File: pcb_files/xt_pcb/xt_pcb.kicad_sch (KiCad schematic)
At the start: 20 parts, among them J1 Conn_01x04_Socket, J2 USB_C_Receptacle_USB2.0_16P, U1 AMS1117-3.3, U2 ATmega32U4-A, U3 USB6B1, Y1 Crystal_GND24_Small

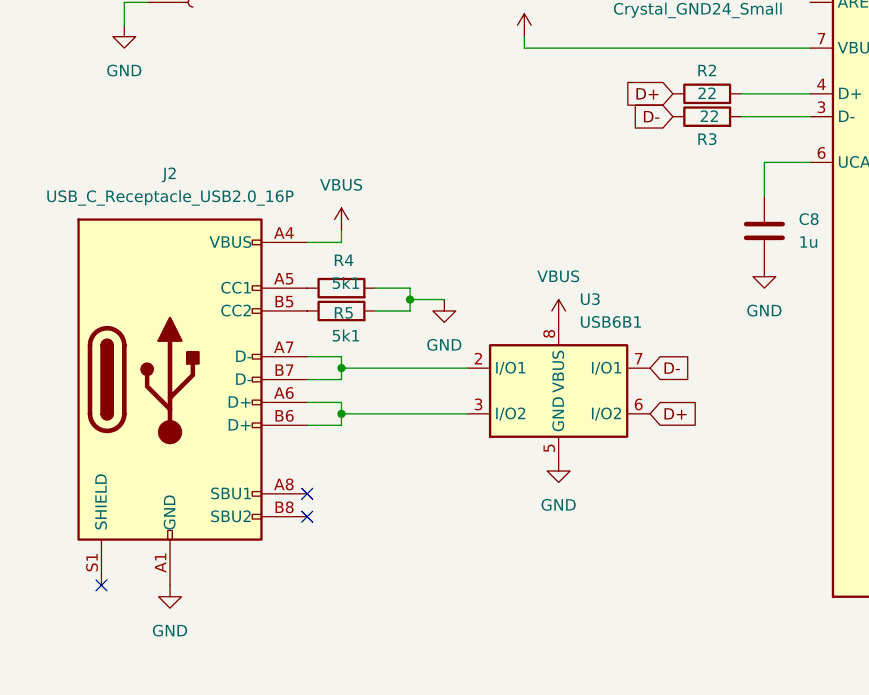
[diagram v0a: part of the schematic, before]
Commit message: finalized files + UDB C4 implementation
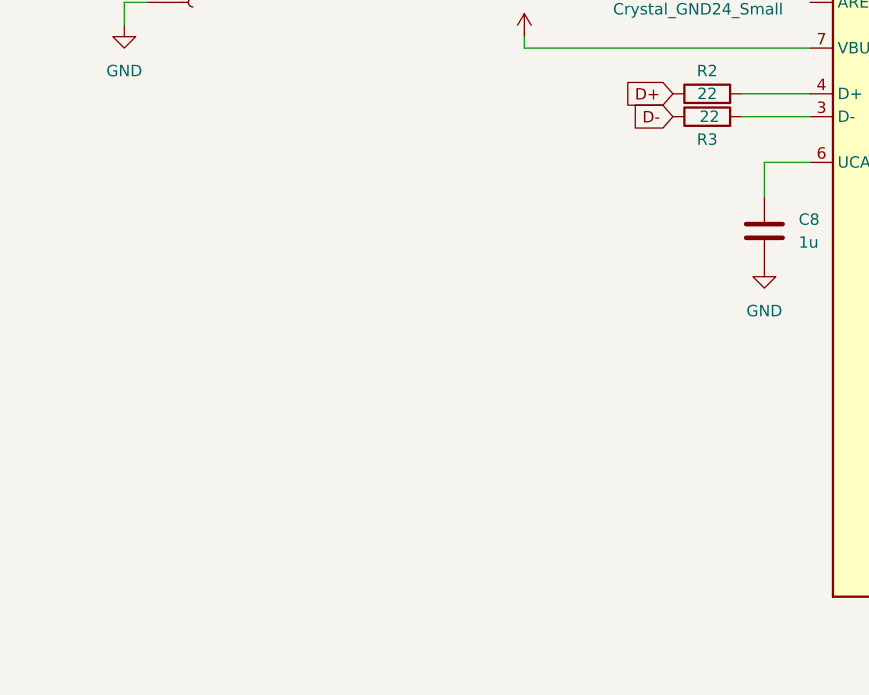
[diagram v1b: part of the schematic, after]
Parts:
- removed J2: USB_C_Receptacle_USB2.0_16P, Connector_USB:USB_C_Receptacle_HRO_TYPE-C-31-M-12, symbol Connector:USB_C_Receptacle_USB2.0_16P
- removed R4, R5: 5k1, Resistor_SMD:R_0402_1005Metric, symbol Device:R
- removed U3: USB6B1, Package_SO:SOIC-8_3.9x4.9mm_P1.27mm, symbol Power_Protection:USB6B1
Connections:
- no-connect marks 3 -> 0

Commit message: basic firmware added
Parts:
- J1: footprint Connector_JST:JST_SH_SM04B-SRSS-TB_1x04-1MP_P1.00mm_Horizontal -> Downloads:MOLEX_781710004
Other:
- moved on the sheet: J1
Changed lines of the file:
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@@
 	(wire
 		(pts
-			(xy 27.94 68.58) (xy 30.48 68.58)
+			(xy 27.94 68.58) (xy 33.02 68.58)
 		)
 		(stroke
@@
 	(wire
 		(pts
-			(xy 30.48 76.2) (xy 27.94 76.2)
+			(xy 33.02 76.2) (xy 27.94 76.2)
+		)
+		(stroke
+			(width 0)
+			(type default)
+		)
+	)
+	(wire
+		(pts
+			(xy 33.02 73.66) (xy 30.48 73.66)
 		)
 		(stroke
@@
 		(pts
 			(xy 29.21 30.48) (xy 29.21 27.94)
+		)
+		(stroke
+			(width 0)
+			(type default)
+		)
+	)
+	(wire
+		(pts
+			(xy 33.02 71.12) (xy 30.48 71.12)
 		)
 		(stroke
@@
 	(symbol
 		(lib_id "Connector:Conn_01x04_Socket")
-		(at 35.56 71.12 0)
+		(at 38.1 71.12 0)
 		(unit 1)
 		(exclude_from_sim no)
@@
 		(dnp no)
 		(property "Reference" "J1"
-			(at 37.592 60.198 0)
+			(at 40.132 60.198 0)
 			(effects
 				(font
@@
 		)
 		(property "Value" "Conn_01x04_Socket"
-			(at 37.592 62.738 0)
-			(effects
-				(font
-					(size 1.27 1.27)
-				)
-				(justify left)
-			)
-		)
-		(property "Footprint" "Connector_JST:JST_SH_SM04B-SRSS-TB_1x04-1MP_P1.00mm_Horizontal"
-			(at 35.56 71.12 0)
-			(effects
-				(font
-					(size 1.27 1.27)
-				)
-				(hide yes)
+			(at 40.132 62.738 0)
+			(effects
+				(font
+					(size 1.27 1.27)
+				)
+				(justify left)
+			)
+		)
+		(property "Footprint" "Downloads:MOLEX_781710004"
+			(at 38.1 71.12 0)
+			(effects
+				(font
+					(size 1.27 1.27)
+				)
 			)
 		)
 		(property "Datasheet" "~"
-			(at 35.56 71.12 0)
+			(at 38.1 71.12 0)
 			(effects
 				(font
@@
 		)
 		(property "Description" "Generic connector, single row, 01x04, script generated"
-			(at 35.56 71.12 0)
-			(effects
-				(font
+			(at 38.1 71.12 0)
+			(effects
+				(font

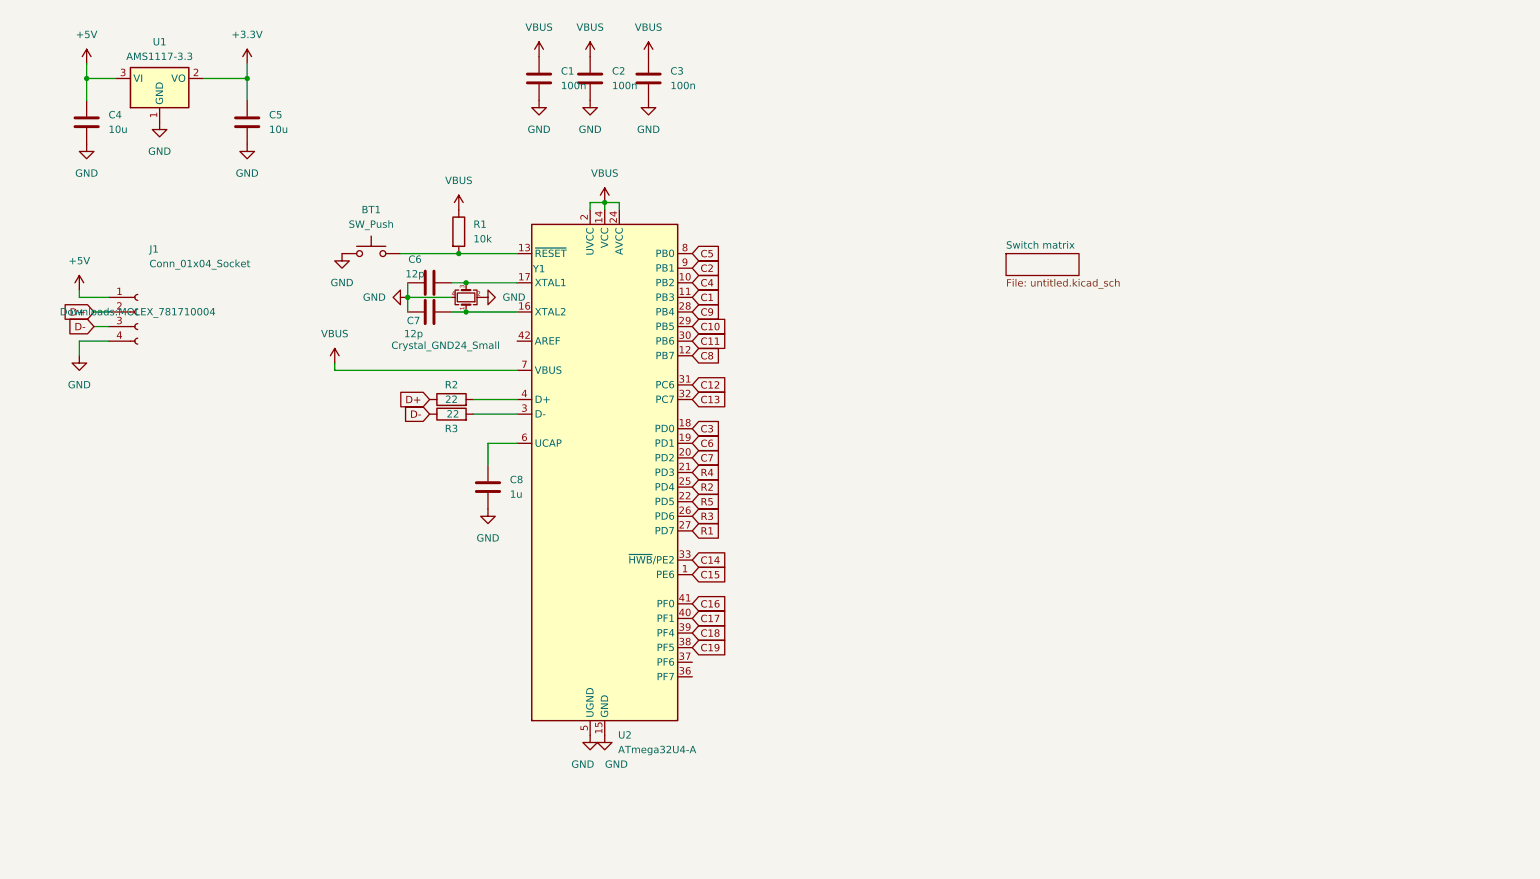
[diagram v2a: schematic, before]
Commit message: new RP2040 pcb
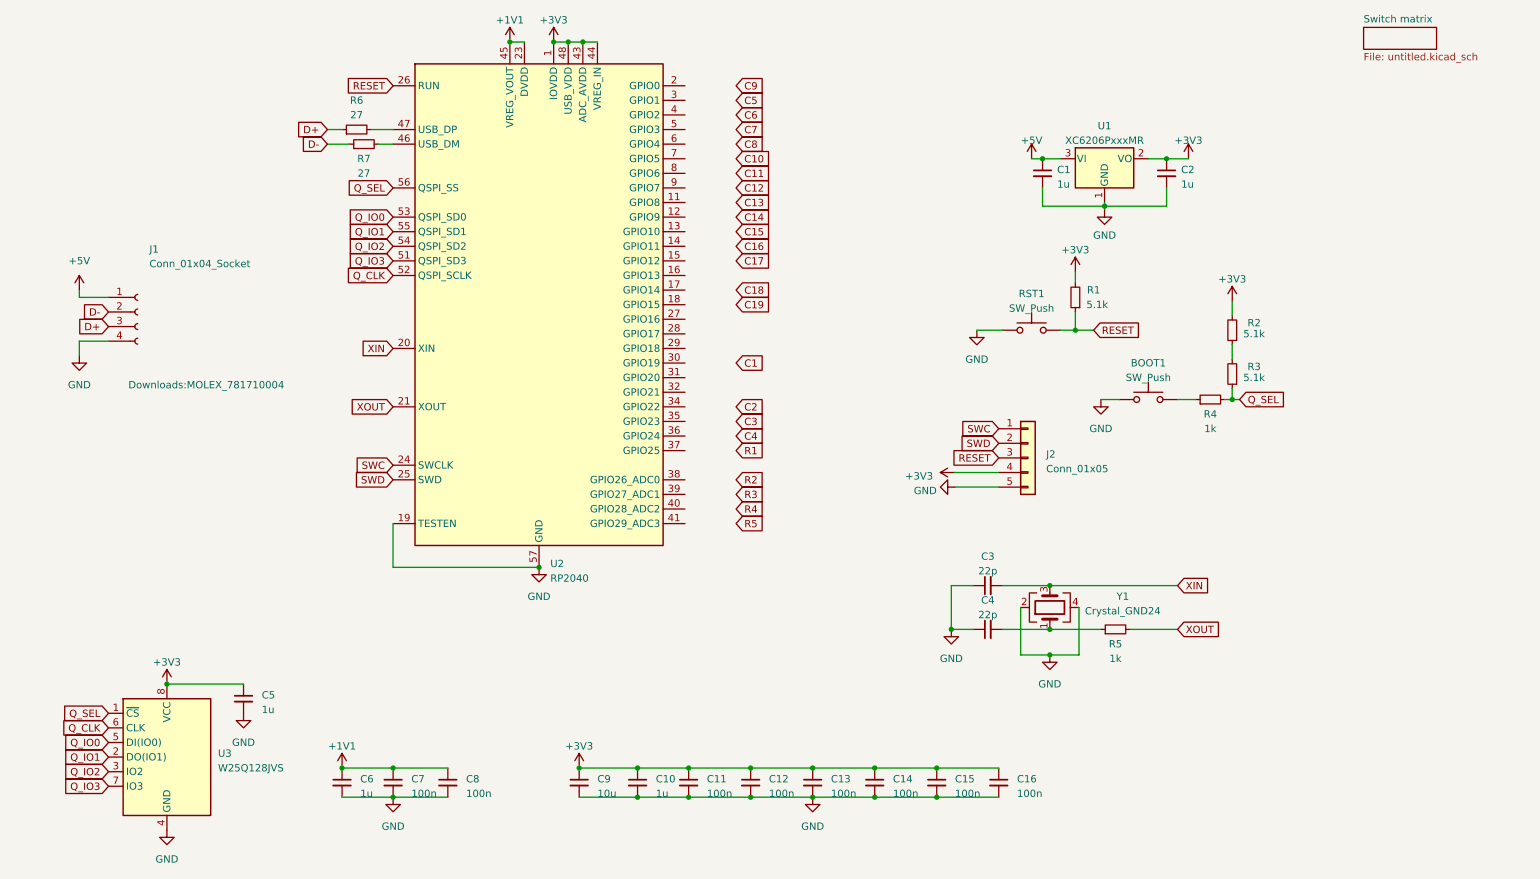
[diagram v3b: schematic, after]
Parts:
- removed BT1: SW_Push, Button_Switch_SMD:SW_SPST_TL3342, symbol Switch:SW_Push
- removed C1, C2, C3: 100n, Capacitor_SMD:C_0402_1005Metric, symbol Device:C
- removed C4, C5: 10u, Capacitor_SMD:C_0603_1608Metric, symbol Device:C
- removed C6, C7: 12p, Capacitor_SMD:C_0402_1005Metric, symbol Device:C
- removed C8: 1u, Capacitor_SMD:C_0402_1005Metric, symbol Device:C
- removed R1: 10k, Resistor_SMD:R_0402_1005Metric, symbol Device:R
- removed R2, R3: 22, Resistor_SMD:R_0402_1005Metric, symbol Device:R
- removed U1: AMS1117-3.3, Package_TO_SOT_SMD:SOT-223-3_TabPin2, symbol Regulator_Linear:AMS1117-3.3
- removed U2: ATmega32U4-A, Package_QFP:TQFP-44_10x10mm_P0.8mm, symbol MCU_Microchip_ATmega:ATmega32U4-A
- removed Y1: Crystal_GND24_Small, Crystal:Crystal_SMD_3225-4Pin_3.2x2.5mm, symbol Device:Crystal_GND24_Small
- added BOOT1, RST1: SW_Push, Button_Switch_SMD:SW_SPST_TL3342, symbol Switch:SW_Push
- added C1, C10, C2, C5, C6: 1u, Capacitor_SMD:C_0402_1005Metric, symbol Device:C_Small
- added C11, C12, C13, C14, C15, C16, C7, C8: 100n, Capacitor_SMD:C_0402_1005Metric, symbol Device:C_Small
- added C3, C4: 22p, Capacitor_SMD:C_0402_1005Metric, symbol Device:C_Small
- added C9: 10u, Capacitor_SMD:C_0603_1608Metric, symbol Device:C_Small
- added J2: Conn_01x05, Connector_PinHeader_2.54mm:PinHeader_1x05_P2.54mm_Vertical, symbol Connector_Generic:Conn_01x05
- added R1, R2, R3: 5.1k, Resistor_SMD:R_0402_1005Metric, symbol Device:R_Small
- added R4, R5: 1k, Resistor_SMD:R_0402_1005Metric, symbol Device:R_Small
- added R6, R7: 27, Resistor_SMD:R_0402_1005Metric, symbol Device:R_Small
- added U1: XC6206PxxxMR, Package_TO_SOT_SMD:SOT-23-3, symbol Regulator_Linear:XC6206PxxxMR
- added U2: RP2040, Package_DFN_QFN:QFN-56-1EP_7x7mm_P0.4mm_EP3.2x3.2mm, symbol MCU_RaspberryPi:RP2040
- added U3: W25Q128JVS, Package_SO:SOIC-8_5.23x5.23mm_P1.27mm, symbol Memory_Flash:W25Q128JVS
- added Y1: Crystal_GND24, Crystal:Crystal_SMD_3225-4Pin_3.2x2.5mm, symbol Device:Crystal_GND24
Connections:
- net +5V: now also C1.1, U1.3 (VI)
- net D+: now also J1.3 (Pin_3), R6.1; no longer J1.2 (Pin_2)
- net D-: now also J1.2 (Pin_2), R7.1; no longer J1.3 (Pin_3)
- net GND: now also BOOT1.1, C1.2, C10.2, C11.2, C12.2, C13.2, C14.2, C15.2, C16.2, C2.2, C3.1, C4.1, C5.2, C6.2, C7.2, C8.2, C9.2, J2.5 (Pin_5), RST1.1, U1.1 (GND), U2.19 (TESTEN), U2.57 (GND), U3.4 (GND), Y1.2, Y1.4
- new net: BOOT1.2, R4.1
- new net: R6.2, U2.47 (USB_DP)
- new net: C4.2, R5.1, Y1.1
- new net: R7.2, U2.46 (USB_DM)
- new net: R2.1, R3.2
- new net +1V1: C6.1, C7.1, C8.1, U2.23 (DVDD), U2.45 (VREG_VOUT), U2.50 (DVDD)
- new net +3V3: C10.1, C11.1, C12.1, C13.1, C14.1, C15.1, C16.1, C2.1, C5.1, C9.1, J2.4 (Pin_4), R1.2, R2.2, U1.2 (VO), U2.1 (IOVDD), U2.10 (IOVDD), U2.22 (IOVDD), U2.33 (IOVDD), U2.42 (IOVDD), U2.43 (ADC_AVDD), U2.44 (VREG_IN), U2.48 (USB_VDD), U2.49 (IOVDD), U3.8 (VCC)
- new net Q_CLK: U2.52 (QSPI_SCLK), U3.6 (CLK)
- new net Q_IO0: U2.53 (QSPI_SD0), U3.5 (DI(IO0))
- new net Q_IO1: U2.55 (QSPI_SD1), U3.2 (DO(IO1))
- new net Q_IO2: U2.54 (QSPI_SD2), U3.3 (IO2)
- new net Q_IO3: U2.51 (QSPI_SD3), U3.7 (IO3)
- new net Q_SEL: R3.1, R4.2, U2.56 (QSPI_SS), U3.1 (~{CS})
- new net RESET: J2.3 (Pin_3), R1.1, RST1.2, U2.26 (RUN)
- new net SWC: J2.1 (Pin_1), U2.24 (SWCLK)
- new net SWD: J2.2 (Pin_2), U2.25 (SWD)
- new net XIN: C3.2, U2.20 (XIN), Y1.3
- new net XOUT: R5.2, U2.21 (XOUT)
